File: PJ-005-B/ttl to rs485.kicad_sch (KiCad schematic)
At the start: 14 parts, among them J7 Pin Header 4 Pin, J8 Pin Header 2 Pin, U13 MAX485CSA+T

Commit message: no message
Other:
- moved on the sheet: R68
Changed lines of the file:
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@@
+	)
+	(junction
+		(at 179.07 77.47)
+		(diameter 0)
+		(color 0 0 0 0)
 	)
 	(junction
@@
 	)
 	(junction
+		(at 179.07 67.31)
+		(diameter 0)
+		(color 0 0 0 0)
+	)
+	(junction
 		(at 185.42 77.47)
 		(diameter 0)
@@
 	)
 	(junction
-		(at 171.45 77.47)
-		(diameter 0)
-		(color 0 0 0 0)
-	)
-	(junction
 		(at 125.73 43.18)
 		(diameter 0)
@@
 	)
 	(junction
-		(at 171.45 67.31)
-		(diameter 0)
-		(color 0 0 0 0)
-	)
-	(junction
 		(at 86.36 76.2)
 		(diameter 0)
@@
 	(wire
 		(pts
-			(xy 167.64 77.47) (xy 171.45 77.47)
+			(xy 167.64 77.47) (xy 179.07 77.47)
 		)
 		(stroke
@@
 	(wire
 		(pts
-			(xy 171.45 76.2) (xy 171.45 77.47)
+			(xy 179.07 76.2) (xy 179.07 77.47)
 		)
 		(stroke
@@
 		)
 	)
+	(wire
+		(pts
+			(xy 179.07 77.47) (xy 185.42 77.47)
+		)
+		(stroke
+			(width 0)
+			(type default)
+		)
+	)
 	(polyline
 		(pts
@@
 	(wire
 		(pts
-			(xy 171.45 67.31) (xy 171.45 68.58)
+			(xy 179.07 67.31) (xy 179.07 68.58)
 		)
 		(stroke
@@
 	(wire
 		(pts
-			(xy 171.45 67.31) (xy 185.42 67.31)
-		)
-		(stroke
-			(width 0)
-			(type default)
-		)
-	)
-	(wire
-		(pts
 			(xy 99.06 43.18) (xy 99.06 48.26)
 		)
@@
 	(wire
 		(pts
+			(xy 179.07 67.31) (xy 185.42 67.31)
+		)
+		(stroke
+			(width 0)
+			(type default)
+		)
+	)
+	(wire
+		(pts
 			(xy 200.66 67.31) (xy 212.09 67.31)
 		)
@@
 	(wire
 		(pts
-			(xy 167.64 67.31) (xy 171.45 67.31)
+			(xy 167.64 67.31) (xy 179.07 67.31)
 		)
 		(stroke
@@
 		(pts
 			(xy 228.6 73.66) (xy 234.95 73.66)
-		)
-		(stroke
-			(width 0)
-			(type default)
-		)
-	)
-	(wire
-		(pts
-			(xy 171.45 77.47) (xy 185.42 77.47)
 		)
 		(stroke
@@
 	(symbol
 		(lib_id "Device:R")
-		(at 171.45 72.39 0)
+		(at 179.07 72.39 0)
 		(unit 1)
 		(exclude_from_sim no)
@@
 		(dnp no)
 		(property "Reference" "R68"
-			(at 166.37 72.39 0)
+			(at 173.99 72.39 0)
 			(effects
 				(font
@@
 		)
 		(property "Value" "120R,1%"
-			(at 172.72 72.39 0)
+			(at 180.34 72.39 0)
 			(effects
 				(font
@@
 		)
 		(property "Footprint" "XaltenFootprints:R0603"
-			(at 169.672 72.39 90)
+			(at 177.292 72.39 90)
 			(effects
 				(font
@@
 		)
 		(property "Datasheet" "~"
-			(at 171.45 72.39 0)
+			(at 179.07 72.39 0)
 			(effects
 				(font
@@
 		)
 		(property "Description" "Resistor"
-			(at 171.45 72.39 0)
-			(effects
-				(font
+			(at 179.07 72.39 0)
+			(effects
+				(font

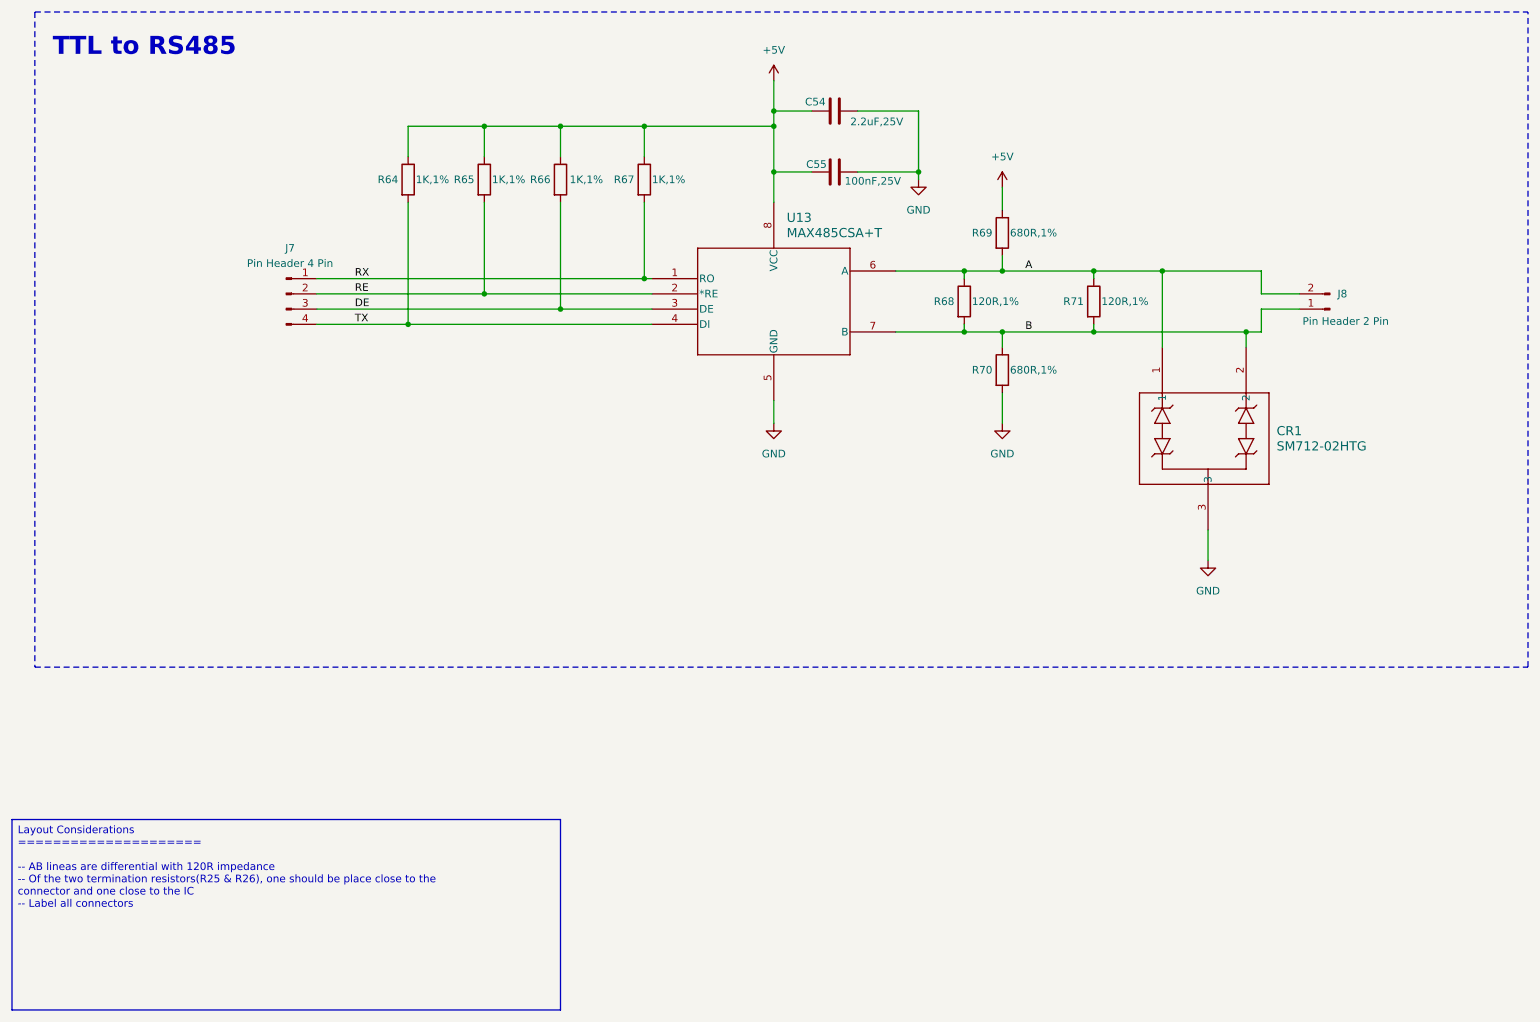
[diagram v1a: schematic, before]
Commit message: Transceiver After Review
-- Added bulk capacitors for -2.5V LDO
-- Added 0R for shorting RE and DE in TTL to RS485
-- Changed the snubber values in transformer primary to 2.2nF and 33R
-- Removed the 10nF and 100K in parallel with the transducer
-- Added 1000uF capacitor for transformer centre tap
-- Added 100pF decoupling capacitor for gate driver IC
--Changed secondary snubber values to 220nF and 680R
-- Changed LC inductor value to 100uH (transformer secondary)
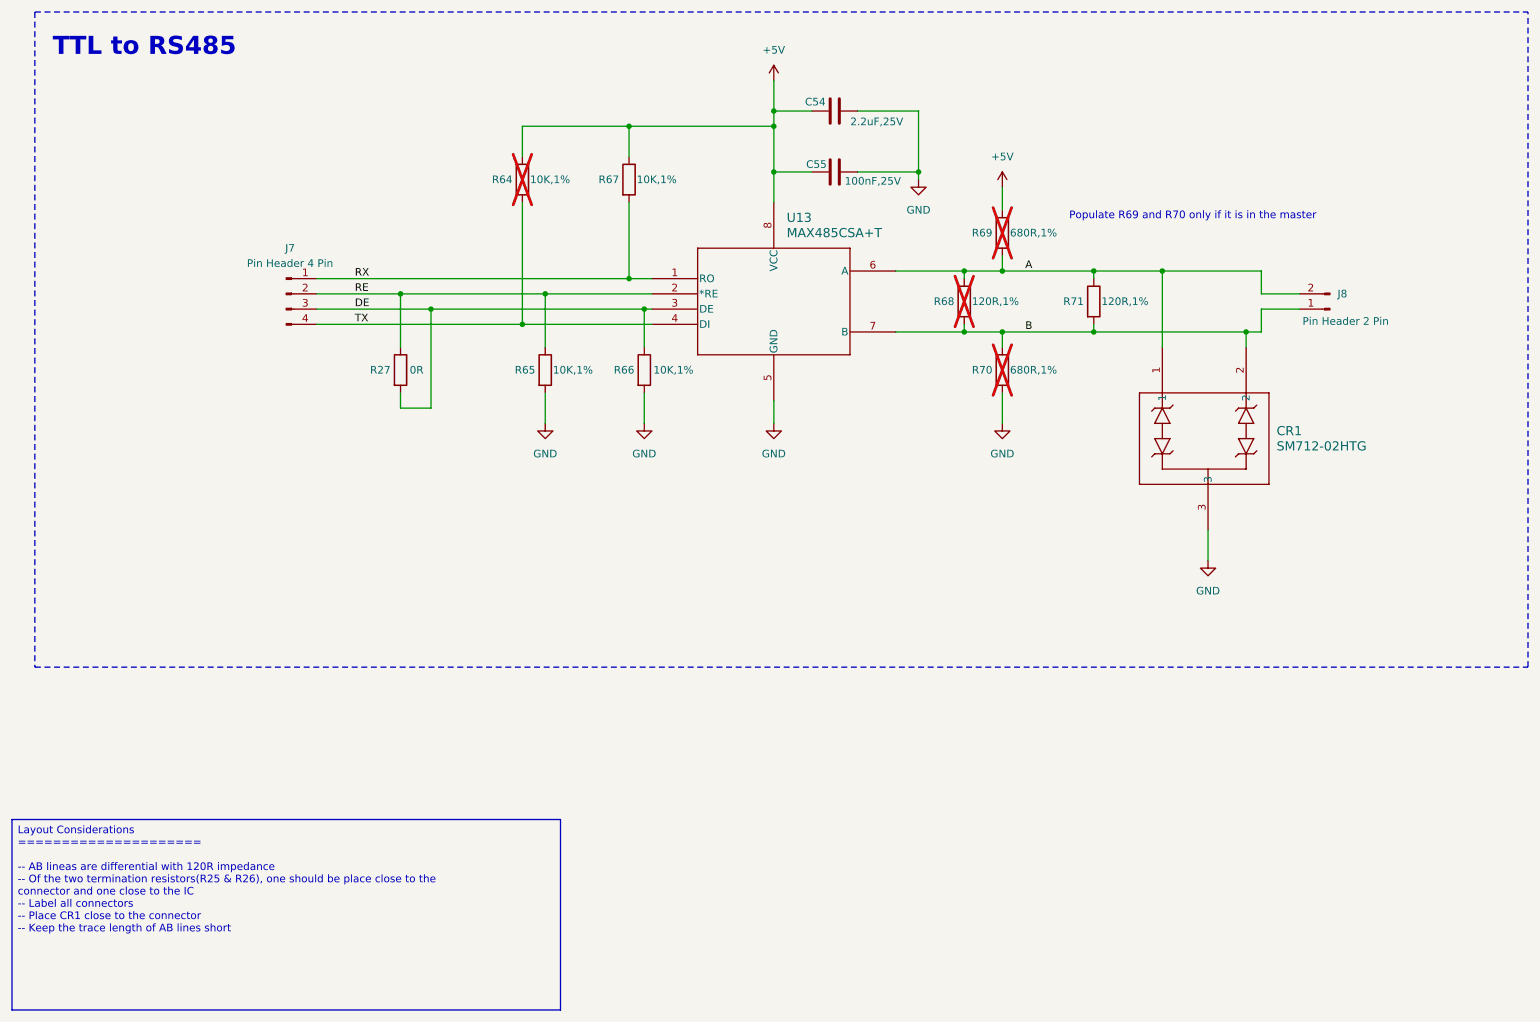
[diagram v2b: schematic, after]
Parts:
- added R27: 0R, XaltenFootprints:R0603, symbol Device:R
- R64: value 1K,1% -> 10K,1%; now not fitted
- R65, R66, R67: value 1K,1% -> 10K,1%
- R68, R69, R70: now not fitted
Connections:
- net +5V: no longer R65.1, R66.1
- net DE: now also R66.1, R27.2; no longer R66.2
- net GND: now also R65.2, R66.2
- net RE: now also R65.1, R27.1; no longer R65.2
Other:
- note added: "Populate R69 and R70 only if it is in the master"
- moved on the sheet: R65, R66, R67
